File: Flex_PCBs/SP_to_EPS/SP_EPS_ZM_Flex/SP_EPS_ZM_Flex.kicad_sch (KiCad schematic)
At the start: 2 parts, among them J1 Conn_01x08_Male, J2 Conn_01x08_Male

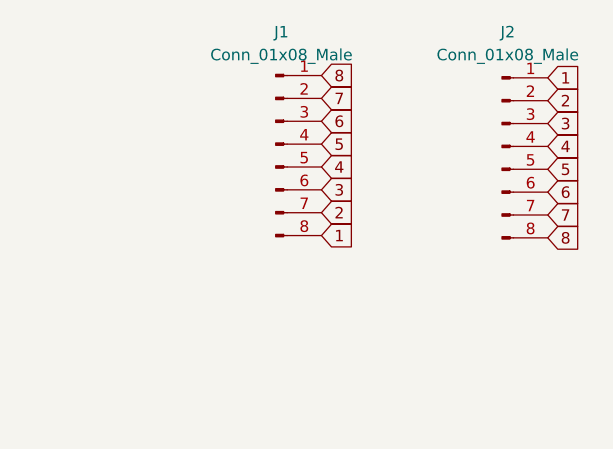
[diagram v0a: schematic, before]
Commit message: replace ZF5S-*-01-T-WT and 2005280040 connectors with T1M-*-F-SH-L-FR connector
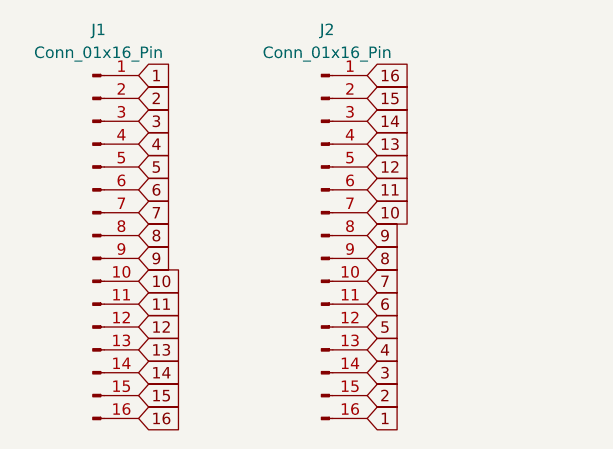
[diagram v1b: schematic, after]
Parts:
- removed J1, J2: Conn_01x08_Male, STS_connector:flexpcb con., symbol Connector:Conn_01x08_Male
- added J1, J2: Conn_01x16_Pin, STS_connector:flexpcb_con_z_minus, symbol Connector:Conn_01x16_Pin
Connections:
- net 1: now also J1.1 (Pin_1), J2.16 (Pin_16)
- net 2: now also J1.2 (Pin_2), J2.15 (Pin_15)
- net 3: now also J1.3 (Pin_3), J2.14 (Pin_14)
- net 4: now also J1.4 (Pin_4), J2.13 (Pin_13)
- net 5: now also J1.5 (Pin_5), J2.12 (Pin_12)
- net 6: now also J1.6 (Pin_6), J2.11 (Pin_11)
- net 7: now also J1.7 (Pin_7), J2.10 (Pin_10)
- net 8: now also J1.8 (Pin_8), J2.9 (Pin_9)
- new net 10: J1.10 (Pin_10), J2.7 (Pin_7)
- new net 11: J1.11 (Pin_11), J2.6 (Pin_6)
- new net 12: J1.12 (Pin_12), J2.5 (Pin_5)
- new net 13: J1.13 (Pin_13), J2.4 (Pin_4)
- new net 14: J1.14 (Pin_14), J2.3 (Pin_3)
- new net 15: J1.15 (Pin_15), J2.2 (Pin_2)
- new net 16: J1.16 (Pin_16), J2.1 (Pin_1)
- new net 9: J1.9 (Pin_9), J2.8 (Pin_8)
